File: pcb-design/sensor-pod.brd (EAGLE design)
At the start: 54.3 x 69.8 mm, 14 parts, among them X1 PH_SENSOR, X10 I2C_3, X11 3.3V, X12 3.3V, X15 MB-LEFT, X16 MB-RIGHT, X2 5V, X3 TURBIDITY, X4 5V, X5 TEMPERATURE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

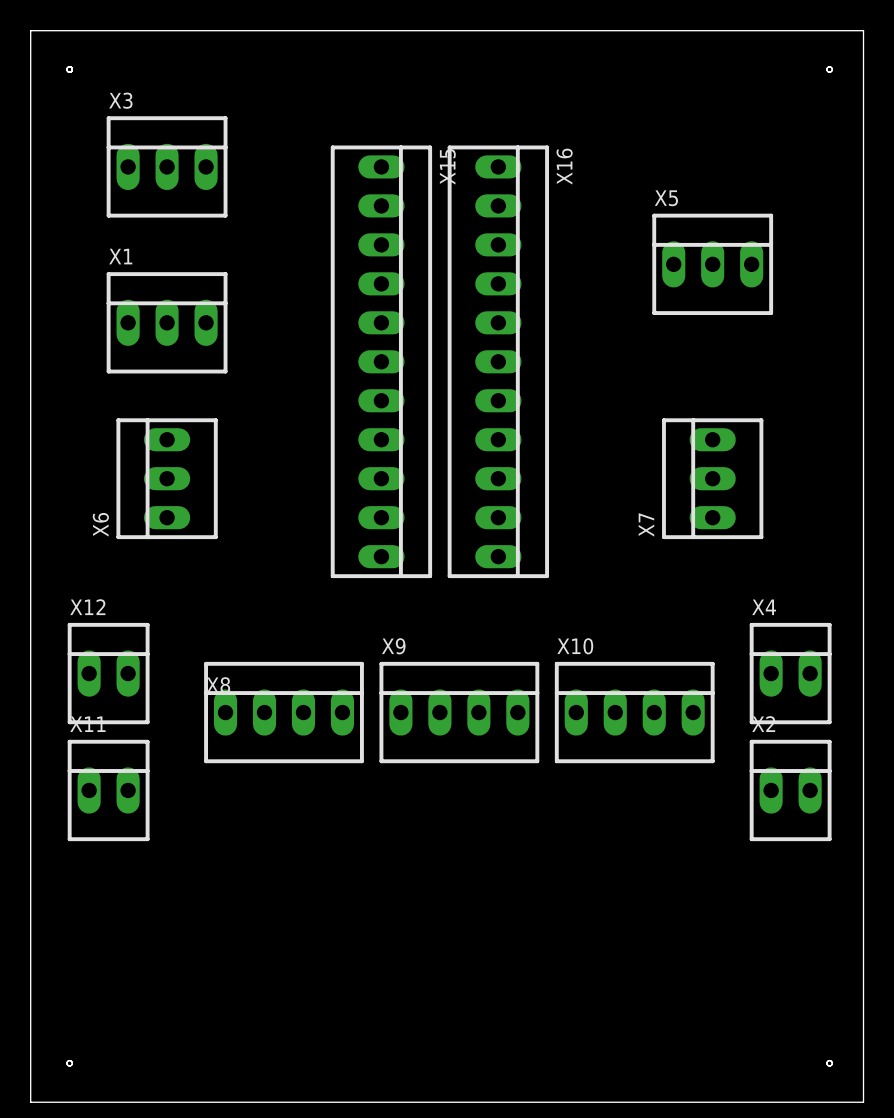
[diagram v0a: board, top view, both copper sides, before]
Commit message: pcb-design: Changed board layout and assigned pins for sensors.
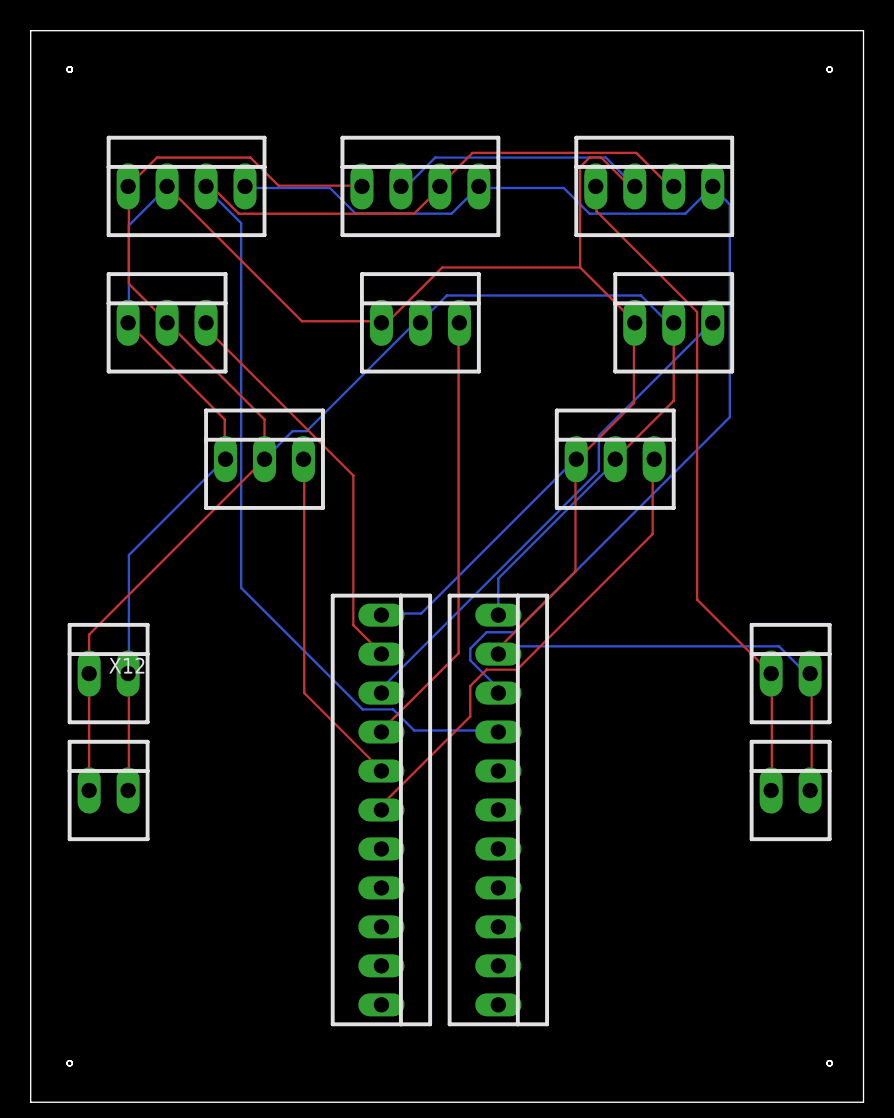
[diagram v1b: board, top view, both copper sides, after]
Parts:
- X10: value I2C_3 -> I2C_5V
- X8: value I2C_1 -> I2C_3.3V
- X9: value I2C_2 -> I2C_3.3V
- moved X8 34.9 mm to (10.2, 59.7)
- moved X9 34.4 mm to (25.4, 59.7)
- moved X10 34.3 mm to (40.6, 59.7)
- moved X15 29.2 mm to (22.9, 19.1)
- moved X16 29.2 mm to (30.5, 19.1)
- moved X3 19.4 mm to (25.4, 50.8)
- moved X7 6.48 mm to (38.1, 41.9), turned to 0 degrees
- moved X6 6.48 mm to (15.2, 41.9), turned to 0 degrees
- moved X5 4.58 mm to (41.9, 50.8)
- renumbered X2 to 1
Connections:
- removed net N$12: X6.3
- removed net N$15: X7.3
- removed net N$3: X1.3
- removed net N$6: X5.3
- removed net N$9: X3.3
- removed net SCL?: X16.4
- removed net SDA?: X16.3
- net PIN_0: now also X1.3
- net PIN_1: now also X5.3
- net PIN_2: now also X3.3
- net PIN_3: now also X6.3
- net PIN_4: now also X7.3
- net SCL: now also X16.4
- net SDA: now also X16.3
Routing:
- net GND: track 0.00 -> 182.2 mm
- net 3.3V: track 0.00 -> 120.3 mm
- net SCL: track 0.00 -> 81.8 mm
- net SDA: track 0.00 -> 75.8 mm
- net 5V: track 0.00 -> 44.1 mm
- net PIN_1: track 0.00 -> 33.1 mm
- net PIN_4: track 0.00 -> 31.4 mm
- net PIN_2: track 0.00 -> 28.8 mm
- net PIN_0: track 0.00 -> 26.3 mm
- net PIN_3: track 0.00 -> 22.5 mm

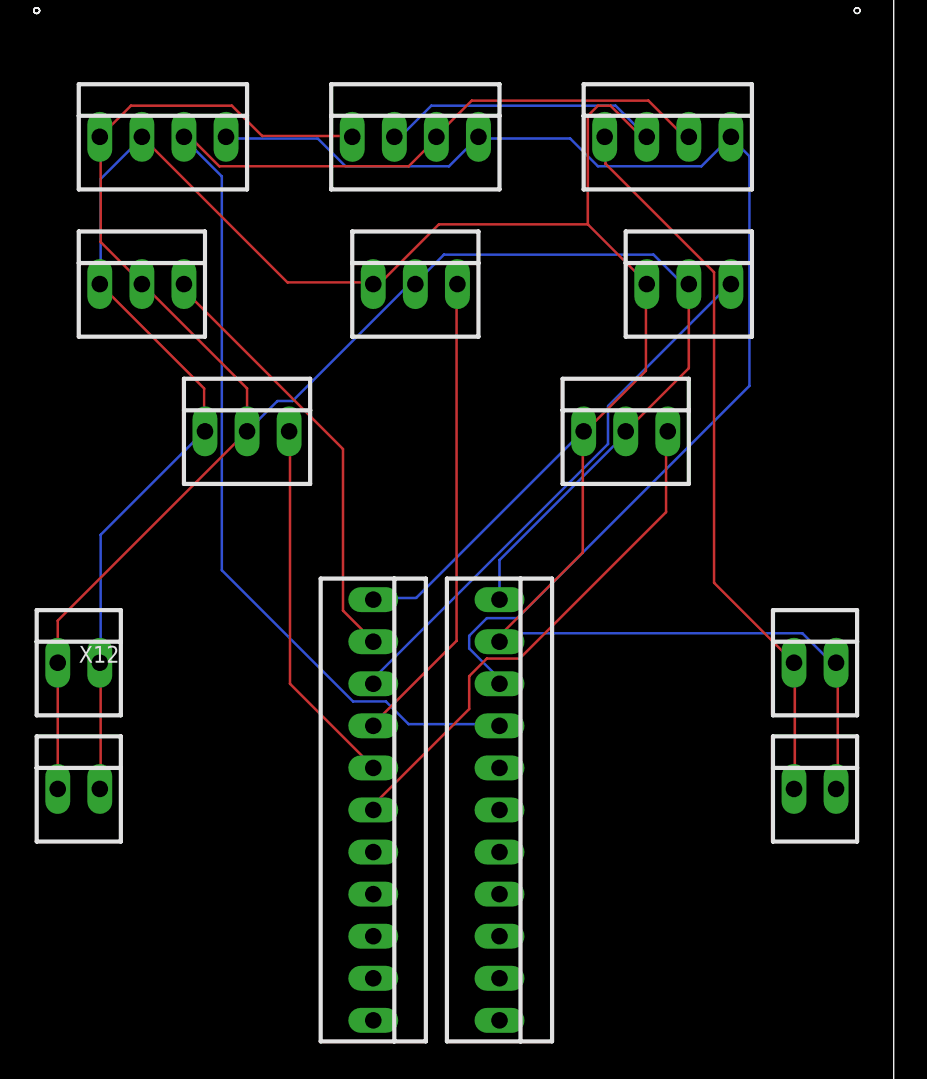
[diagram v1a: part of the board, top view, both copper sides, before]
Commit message: Sensor pod: Fix temp sensor code to use P8 + Changed PCB to match
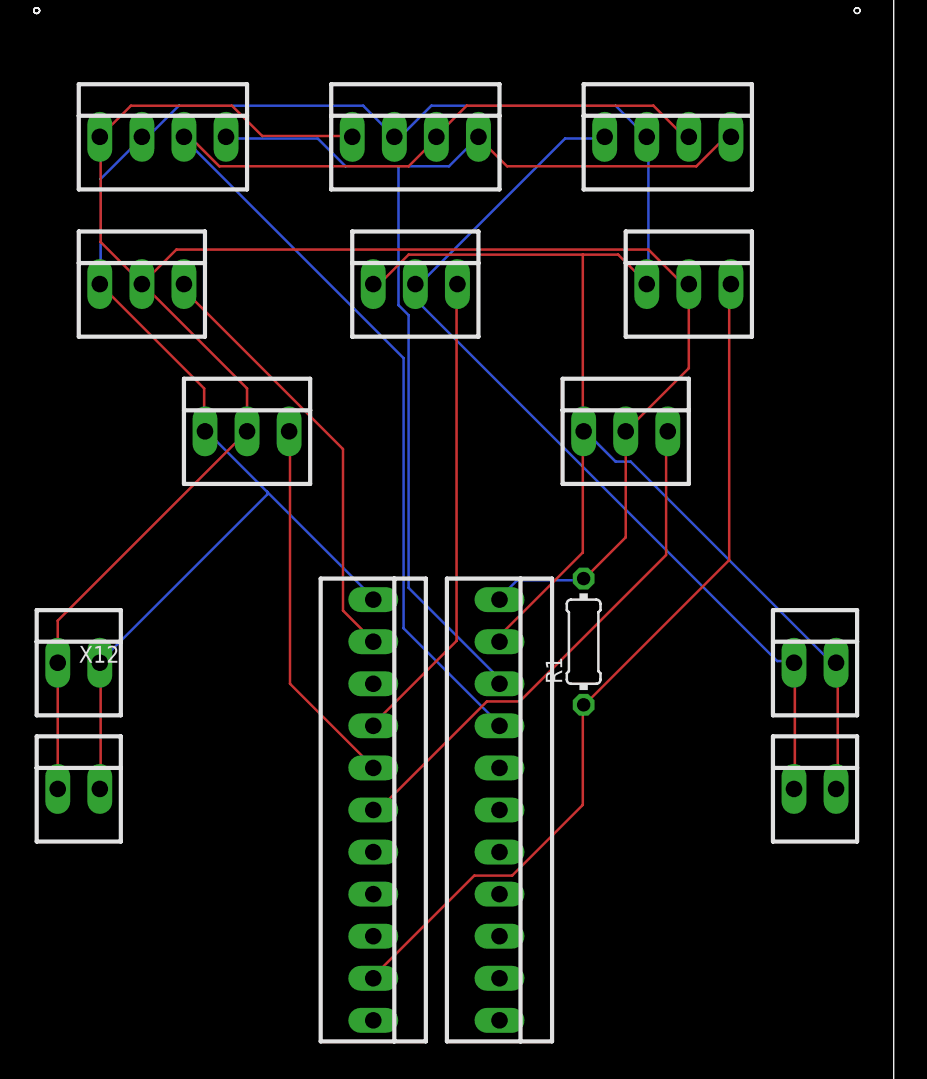
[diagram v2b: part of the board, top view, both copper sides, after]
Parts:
- added R1: 4.7k, rcl:0204/7
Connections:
- net 3.3V: now also R1.2; no longer X3.2
- net 5V: now also X3.2
- net PIN_1: no longer X5.3
- net PIN_8: now also R1.1, X5.3
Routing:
- net PIN_8: track 0.00 -> 52.2 mm
- net PIN_1: track 33.1 -> 0.00 mm
- net 5V: track 44.1 -> 55.7 mm
- net GND: track 182.2 -> 172.9 mm
- net SDA: track 75.8 -> 67.2 mm
- net 3.3V: track 120.3 -> 125.5 mm
- net SCL: track 81.8 -> 77.1 mm

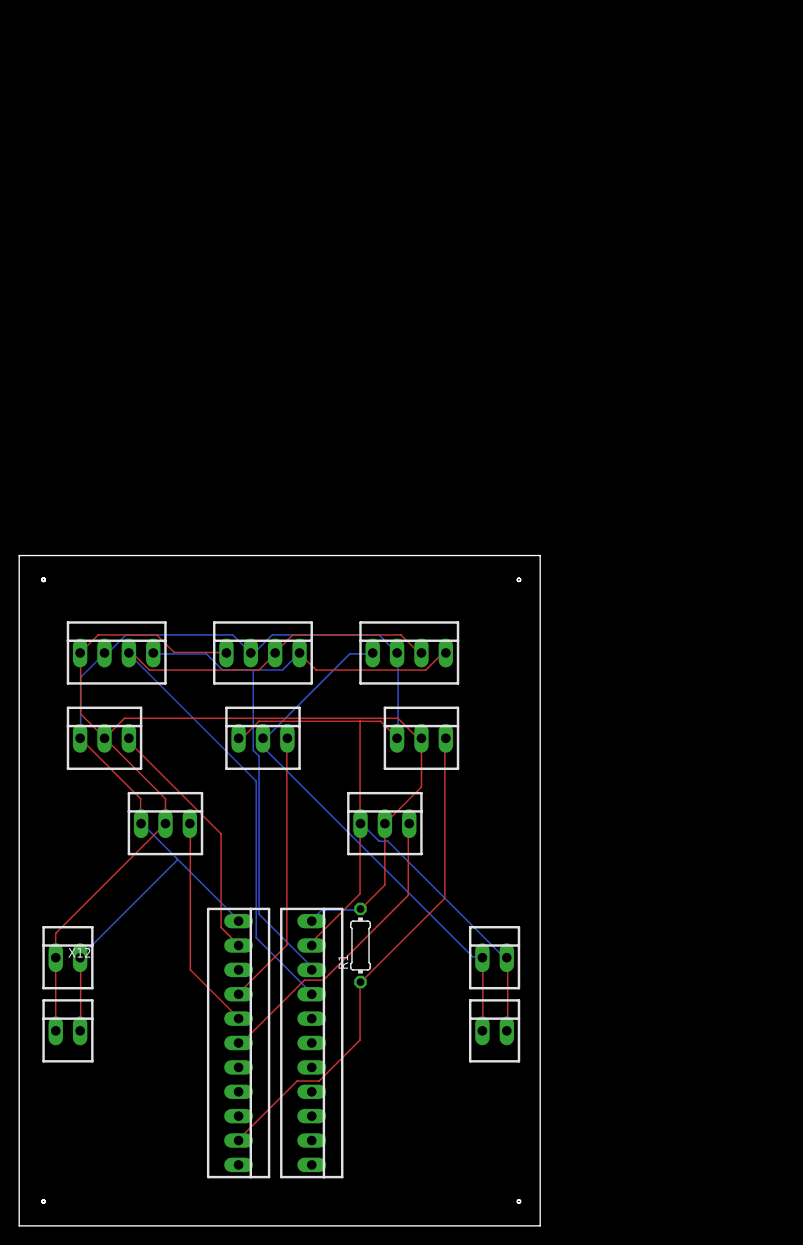
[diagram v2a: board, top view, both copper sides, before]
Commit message: pcb-design: Draft 2 Added LDR and power LED's + Changed board size/placement
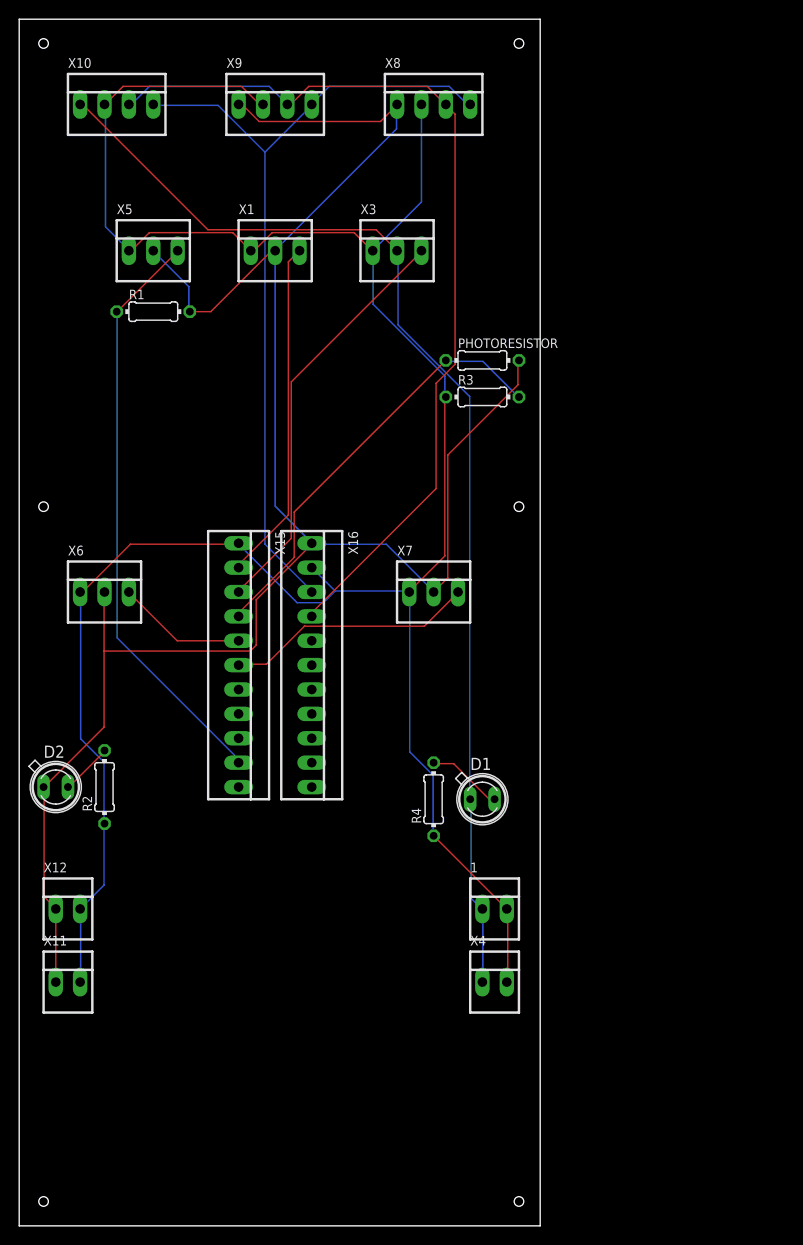
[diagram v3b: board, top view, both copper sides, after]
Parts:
- added D1: 5V_LED, led:SFH482
- added D2: 3.3V_LED, led:SFH482
- added PHOTORESISTOR, R2, R3, R4: (no value), rcl:0204/7
- moved R1 69.5 mm to (14.0, 95.2), turned to 0 degrees
- moved X8 66.0 mm to (43.2, 116.8)
- moved X10 64.8 mm to (10.2, 116.8)
- moved X5 58.0 mm to (14.0, 101.6)
- moved X9 57.2 mm to (26.7, 116.8)
- moved X1 53.8 mm to (26.7, 101.6)
- moved X3 52.7 mm to (39.4, 101.6)
- moved X15 39.4 mm to (22.9, 58.4)
- moved X16 39.4 mm to (30.5, 58.4)
- moved X6 25.0 mm to (8.89, 66.0)
- moved X7 24.7 mm to (43.2, 66.0)
- moved 1 12.7 mm to (49.5, 33.0)
- moved X12 5.08 mm to (5.08, 33.0)
- moved X11 5.08 mm to (5.08, 25.4)
- moved X4 2.54 mm to (49.5, 25.4)
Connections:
- new net N$1: D1.K, R4.2
- new net N$2: D2.K, R2.2
- net 3.3V: now also D2.A, PHOTORESISTOR.2
- net 5V: now also D1.A
- net GND: now also R2.1, R3.1, R4.1
- net PIN_1: now also X3.3
- net PIN_2: now also PHOTORESISTOR.1, R3.2; no longer X3.3
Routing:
- net 3.3V: track 125.5 -> 205.8 mm
- net GND: track 172.9 -> 251.3 mm
- net 5V: track 55.7 -> 119.3 mm
- net PIN_1: track 0.00 -> 43.5 mm
- net SDA: track 67.2 -> 86.7 mm
- net SCL: track 77.1 -> 96.1 mm
- net PIN_2: track 28.8 -> 44.8 mm
- net PIN_0: track 26.3 -> 35.7 mm
- net PIN_8: track 52.2 -> 61.3 mm
- net PIN_3: track 22.5 -> 13.6 mm
- net N$1: track 0.00 -> 7.96 mm
- net N$2: track 0.00 -> 5.59 mm
- net PIN_4: track 31.6 -> 26.1 mm
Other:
- board size 54.3 x 69.8 mm -> 54.3 x 125.7 mm

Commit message: pcd-design: Decreased distance between components and microbit interface. Increased PCB size.
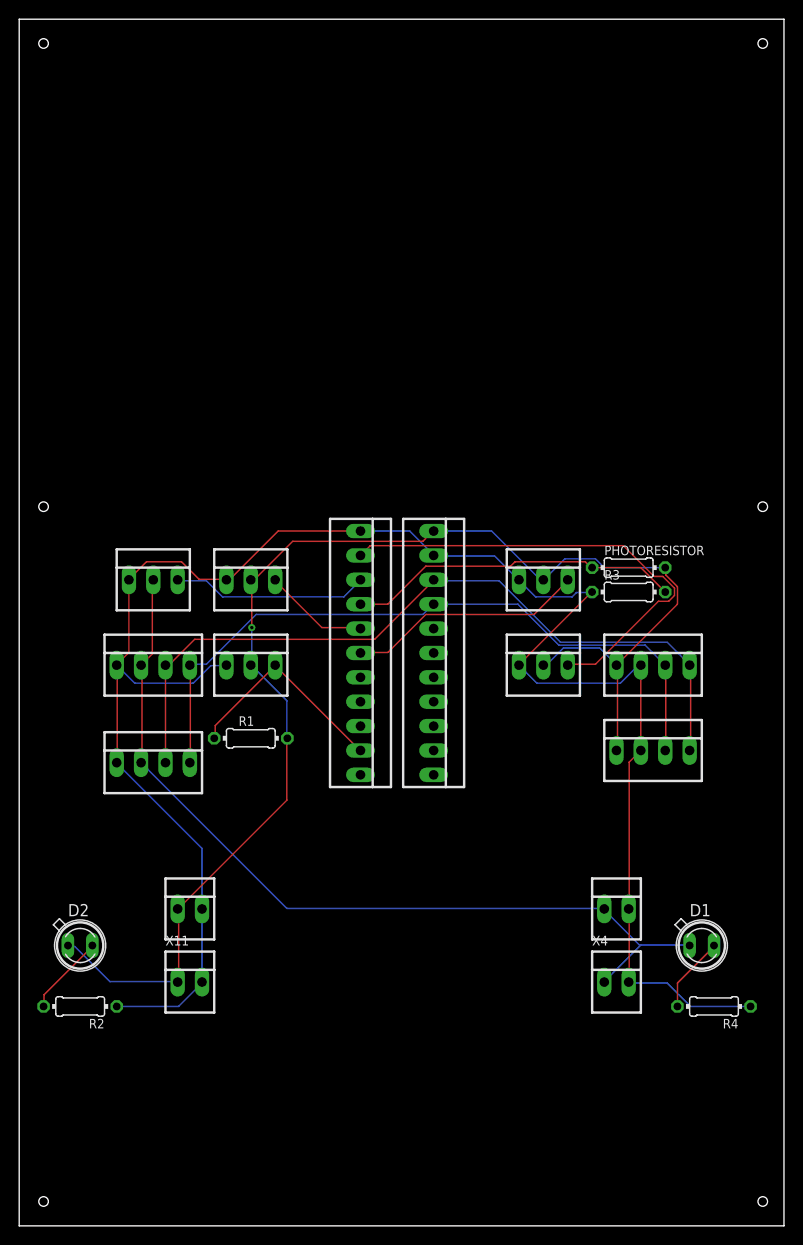
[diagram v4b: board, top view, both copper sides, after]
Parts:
- added X2: I2C_5V, con-molex:22-23-2041
- R3: value (none) -> 10k
- moved X9 78.0 mm to (66.0, 49.5)
- moved X10 68.7 mm to (14.0, 48.3)
- moved X8 62.7 mm to (66.0, 58.4)
- moved X1 51.4 mm to (54.6, 58.4)
- moved R1 45.6 mm to (24.1, 50.8)
- moved X5 44.4 mm to (24.1, 58.4)
- moved X3 42.7 mm to (14.0, 67.3)
- moved R4 36.3 mm to (72.4, 22.9), turned to 180 degrees
- moved D1 27.5 mm to (71.1, 29.2)
- moved PHOTORESISTOR 26.4 mm to (63.5, 68.6)
- moved R3 25.4 mm to (63.5, 66.0)
- moved R2 23.0 mm to (6.35, 22.9), turned to 180 degrees
- moved D2 16.7 mm to (6.35, 29.2)
- moved X6 15.3 mm to (24.1, 67.3)
- moved X15 12.8 mm to (35.6, 59.7)
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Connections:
- net 5V: now also X10.2, X2.2; no longer X10.1
- net GND: now also X10.1, X2.1; no longer X10.2
- net SCL: now also X10.4, X2.4; no longer X10.3
- net SDA: now also X10.3, X2.3; no longer X10.4
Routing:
- net 3.3V: track 205.8 -> 141.6 mm, vias 0 -> 1
- net GND: track 251.3 -> 196.6 mm
- net PIN_8: track 61.3 -> 22.8 mm
- net 5V: track 119.3 -> 90.3 mm
- net PIN_1: track 43.5 -> 20.5 mm
- net SCL: track 96.1 -> 74.0 mm
- net PIN_0: track 35.7 -> 49.9 mm
- net PIN_2: track 44.8 -> 34.9 mm
- net SDA: track 86.7 -> 81.3 mm
- net N$2: track 5.59 -> 8.48 mm
- net PIN_3: track 13.6 -> 11.1 mm
- net PIN_4: track 26.1 -> 24.8 mm
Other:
- board size 54.3 x 125.7 mm -> 79.7 x 125.7 mm
